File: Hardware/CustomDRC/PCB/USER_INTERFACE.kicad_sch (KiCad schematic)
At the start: 35 parts, among them J501 Conn_01x05, J504 Conn_01x05, Q501 AO3401A, Q502 AO3400A, U501 ESD224DQA, U502 ESD224DQA

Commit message: Update - finished schematic for revision A
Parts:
- removed Q501: AO3401A, Package_TO_SOT_SMD:SOT-23, symbol Transistor_FET:AO3401A
- removed Q502: AO3400A, Package_TO_SOT_SMD:SOT-23, symbol Transistor_FET:AO3400A
- added J502: JST-PH-2.0-02, Connector_JST:JST_PH_B2B-PH-K_1x02_P2.00mm_Vertical, symbol Connector_Generic:Conn_01x02
- added Q501: AO3400A, Package_TO_SOT_SMD:SOT-23, symbol Transistor_FET:AO3400A
- C501, C502, C503, C504, C505, C506: LCSC (none) -> C14663; MPN (none) -> CC0603KRX7R9BB104; Manufacturer (none) -> YAGEO
- J501, J504: value Conn_01x05 -> JST-PH-2.0-05; LCSC (none) -> C157993; MPN (none) -> B5B-PH-K-S(LF)(SN); Manufacturer (none) -> JST
- R501, R503: value 10k -> 330R; LCSC (none) -> C23138; MPN (none) -> 0603WAF3300T5E; Manufacturer (none) -> UNI-ROYAL(Uniroyal Elec)
- R502, R504, R510, R511, R512, R515: value 330R -> 10k; LCSC (none) -> C25804; MPN (none) -> 0603WAF1002T5E; Manufacturer (none) -> UNI-ROYAL(Uniroyal Elec)
- R505, R506, R507, R508, R509, R513, R514: LCSC (none) -> C25804; MPN (none) -> 0603WAF1002T5E; Manufacturer (none) -> UNI-ROYAL(Uniroyal Elec)
- TP508: footprint TestPoint:TestPoint_Pad_D1.5mm -> TestPoint:TestPoint_Keystone_5000-5004_Miniature; LCSC (none) -> C5199801; MPN (none) -> RH-5001; Manufacturer (none) -> ronghe; now in the parts list
- U501, U502: LCSC (none) -> C5199157; MPN (none) -> RClAMP3324P-ES; Manufacturer (none) -> ElecSuper
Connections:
- net VCC_ENCODER is gone; now on net VCC: R506.2, R507.2, R508.2, R509.2
- net ENCODER_1_A: no longer R506.1
- net ENCODER_1_B: now also R502.1; no longer R502.2, R507.1
- net ENCODER_1_SW: now also R512.1; no longer R512.2, R513.1
- net ENCODER_2_A: no longer R509.1
- net ENCODER_2_B: now also R510.1; no longer R508.1, R510.2
- net ENCODER_2_SW: now also R515.1; no longer R514.1, R515.2
- net ENC_1_A: now also R506.1
- net ENC_1_B: now also R502.2, R507.1; no longer R502.1
- net ENC_1_SW: now also R512.2, R513.1; no longer R512.1
- net ENC_2_B: now also R508.1, R510.2; no longer R510.1
- net ENC_2_SW: now also R514.1, R515.2; no longer R515.1
- net GND: now also R505.1, Q501.2 (S); no longer R503.2
- net VCC: no longer R501.1
- net at R501.2: now also J502.2 (Pin_2)
- net ENCODER_PWR_EN: no longer names the net of R505.2
- net ENCODER_PWR_EN: now also R503.2, Q501.1 (G); no longer R503.1
- net ENC_3_A renamed ENC_2_A
- net ENC_2_A: now also R509.1
- new net: J502.1 (Pin_1), Q501.3 (D)
- new net +5V: R501.1
- new net LED_PWM: R503.1
- no-connect marks 3 -> 2
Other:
- note added: "OUTPUT LED CONNECTOR"
- company: (none) -> JS HW
- title: (none) -> CDRC - Custom DRC for Audison AC Link
- moved on the sheet: C501, C502, C503, C504, C505, C506, J501, J504, R506, R507, R508, R509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

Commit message: Sync HW changes for V1 PCB
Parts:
- added R516: 330R, Resistor_SMD:R_1206_3216Metric_Pad1.30x1.75mm_HandSolder, symbol Device:R_Small
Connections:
- net +5V is gone; now on net VCC: R501.1
- net VCC: now also R516.2
- net at J502.2 (Pin_2), R501.2: now also R516.1
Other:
- note added: "DNP - USE IF THERMAL ISSUE"
- note added: "I = 10mA P = 0.033W"
- moved on the sheet: C501, C502, C503, C504, C505, C506, J501, J504, R501, R502, R504, R506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

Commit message: Sync before making breaking changes to RS485 comms protocl and method
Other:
- title: CDRC - Custom DRC for Audison AC Link -> CDRC - Custom DRC for Bit 10D
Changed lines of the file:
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@@
 	(paper "A4")
 	(title_block
-		(title "CDRC - Custom DRC for Audison AC Link")
-		(date "03-09-2024")
-		(rev "A")
+		(title "CDRC - Custom DRC for Bit 10D")
+		(date "01-11-2024")
+		(rev "B")
 		(company "JS HW")
 	)

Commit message: Sync changes to Rev B HW
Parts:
- removed J501, J504: JST-PH-2.0-05, Connector_JST:JST_PH_B5B-PH-K_1x05_P2.00mm_Vertical, symbol Connector_Generic:Conn_01x05
- removed J502: JST-PH-2.0-02, Connector_JST:JST_PH_B2B-PH-K_1x02_P2.00mm_Vertical, symbol Connector_Generic:Conn_01x02
- removed TP507: TestPoint_Small, TestPoint:TestPoint_Pad_D1.5mm, symbol Connector:TestPoint_Small
- added J501, J504: JST_PH_S5B-PH-SM4, Connector_JST:JST_PH_S5B-PH-SM4-TB_1x05-1MP_P2.00mm_Horizontal, symbol Connector_Generic_MountingPin:Conn_01x05_MountingPin
- added J502: ST_PH_S2B-PH-SM4, Connector_JST:JST_PH_S2B-PH-SM4-TB_1x02-1MP_P2.00mm_Horizontal, symbol Connector_Generic_MountingPin:Conn_01x02_MountingPin
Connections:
- net ENC_1_A: now also J501.1 (Pin_1)
- net ENC_1_B: now also J501.3 (Pin_3)
- net ENC_1_SW: now also J501.5 (Pin_5)
- net ENC_2_A: now also J504.1 (Pin_1)
- net ENC_2_B: now also J504.3 (Pin_3)
- net ENC_2_SW: now also J504.5 (Pin_5)
- net GND: now also J501.2 (Pin_2), J501.4 (Pin_4), J504.2 (Pin_2), J504.4 (Pin_4)
- net at Q501.3 (D): now also J502.1 (Pin_1)
- net at R501.2, R516.1: now also J502.2 (Pin_2)
- new net MNT: J501.MP (MountPin), J502.MP (MountPin), J504.MP (MountPin)
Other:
- note added: "ENCODERS"
- note added: "LED CONTROL"
- moved on the sheet: Q501, R501, R503, R505, R516

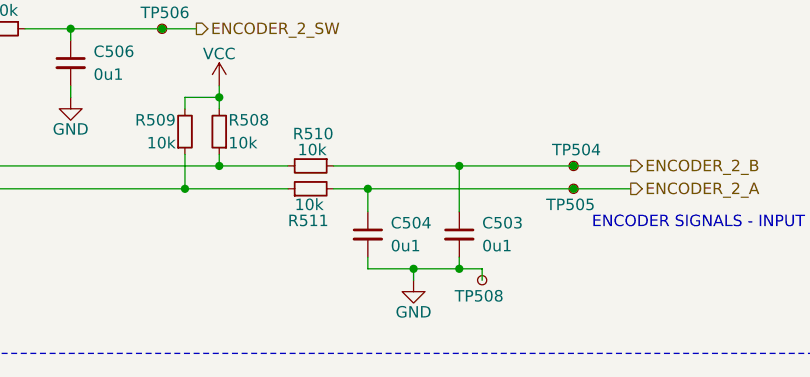
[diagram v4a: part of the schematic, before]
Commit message: Added board renders and PDF plots
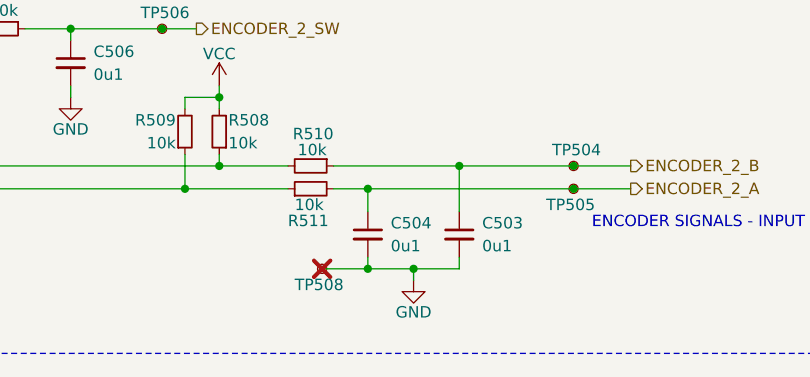
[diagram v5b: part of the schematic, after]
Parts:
- TP508: now not fitted; now left out of the parts list
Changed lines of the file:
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@@
 	)
 	(junction
+		(at 167.64 147.32)
+		(diameter 0)
+		(color 0 0 0 0)
+	)
+	(junction
 		(at 121.92 77.47)
 		(diameter 0)
@@
 	)
 	(junction
-		(at 177.8 147.32)
-		(diameter 0)
-		(color 0 0 0 0)
-	)
-	(junction
 		(at 120.65 120.65)
 		(diameter 0)
@@
 	(wire
 		(pts
-			(xy 172.72 147.32) (xy 167.64 147.32)
-		)
-		(stroke
-			(width 0)
-			(type default)
-		)
-	)
-	(wire
-		(pts
 			(xy 87.63 41.91) (xy 87.63 43.18)
 		)
@@
 	(wire
 		(pts
-			(xy 177.8 147.32) (xy 180.34 147.32)
+			(xy 162.56 147.32) (xy 167.64 147.32)
 		)
 		(stroke
@@
 	(wire
 		(pts
-			(xy 180.34 148.59) (xy 180.34 147.32)
+			(xy 167.64 147.32) (xy 172.72 147.32)
 		)
 		(stroke
@@
 	(symbol
 		(lib_id "Connector:TestPoint_Small")
-		(at 180.34 148.59 0)
+		(at 162.56 147.32 0)
 		(mirror x)
 		(unit 1)
 		(exclude_from_sim no)
-		(in_bom yes)
+		(in_bom no)
 		(on_board yes)
-		(dnp no)
+		(dnp yes)
 		(property "Reference" "TP508"
-			(at 177.292 150.368 0)
+			(at 159.512 149.098 0)
 			(effects
 				(font
@@
 		)
 		(property "Value" "TestPoint_Small"
-			(at 181.61 147.3201 0)
+			(at 163.83 146.0501 0)
 			(effects
 				(font
@@
 		)
 		(property "Footprint" "TestPoint:TestPoint_Keystone_5000-5004_Miniature"
-			(at 185.42 148.59 0)
+			(at 167.64 147.32 0)
 			(effects
 				(font
@@
 		)
 		(property "Datasheet" "~"
-			(at 185.42 148.59 0)
+			(at 167.64 147.32 0)
 			(effects
 				(font
@@
 		)
 		(property "Description" "test point"
-			(at 180.34 148.59 0)
+			(at 162.56 147.32 0)
 			(effects
 				(font
@@
 		)
 		(property "LCSC" "C5199801"
-			(at 180.34 148.59 0)
+			(at 162.56 147.32 0)
 			(effects
 				(font
@@
 		)
 		(property "MPN" " RH-5001"
-			(at 180.34 148.59 0)
+			(at 162.56 147.32 0)
 			(effects
 				(font
@@
 		)
 		(property "Manufacturer" " ronghe"
-			(at 180.34 148.59 0)
+			(at 162.56 147.32 0)
 			(effects
 				(font

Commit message: Update HW folder with latest work on rev B
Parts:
- J501, J504: LCSC (none) -> C265104; MPN (none) -> S5B-PH-SM4-TB(LF)(SN); Manufacturer (none) -> JST
- J502: value ST_PH_S2B-PH-SM4 -> JST_PH_S2B-PH-SM4; LCSC (none) -> C295747; MPN (none) -> S2B-PH-SM4-TB(LF)(SN); Manufacturer (none) -> JST
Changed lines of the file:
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@@
 	(title_block
 		(title "CDRC - Custom DRC for Bit 10D")
-		(date "01-11-2024")
+		(date "25-11-2024")
 		(rev "B")
 		(company "JS HW")
@@
 			)
 		)
-		(property "Value" "ST_PH_S2B-PH-SM4"
+		(property "Value" "JST_PH_S2B-PH-SM4"
 			(at 97.79 39.116 0)
 			(effects
@@
 			)
 		)
+		(property "Manufacturer" "JST"
+			(at 95.25 41.91 0)
+			(effects
+				(font
+					(size 1.27 1.27)
+				)
+				(hide yes)
+			)
+		)
+		(property "MPN" " S2B-PH-SM4-TB(LF)(SN)"
+			(at 95.25 41.91 0)
+			(effects
+				(font
+					(size 1.27 1.27)
+				)
+				(hide yes)
+			)
+		)
+		(property "LCSC" "C295747"
+			(at 95.25 41.91 0)
+			(effects
+				(font
+					(size 1.27 1.27)
+				)
+				(hide yes)
+			)
+		)
 		(pin "1"
 		)
@@
 			)
 		)
+		(property "LCSC" "C265104"
+			(at 73.66 130.81 0)
+			(effects
+				(font
+					(size 1.27 1.27)
+				)
+				(hide yes)
+			)
+		)
+		(property "MPN" "S5B-PH-SM4-TB(LF)(SN)"
+			(at 73.66 130.81 0)
+			(effects
+				(font
+					(size 1.27 1.27)
+				)
+				(hide yes)
+			)
+		)
+		(property "Manufacturer" "JST"
+			(at 73.66 130.81 0)
+			(effects
+				(font
+					(size 1.27 1.27)
+				)
+				(hide yes)
+			)
+		)
 		(pin "3"
 		)
@@
 			(at 73.66 87.63 0)
 			(effects
+				(font
+					(size 1.27 1.27)
+				)
+				(hide yes)
+			)
+		)
+		(property "LCSC" "C265104"
+			(at 73.66 87.63 0)
+			(effects
+				(font
+					(size 1.27 1.27)
+				)
+				(hide yes)
+			)
+		)
+		(property "MPN" "S5B-PH-SM4-TB(LF)(SN)"
+			(at 73.66 87.63 0)
+			(effects
+				(font
+					(size 1.27 1.27)
+				)
+				(hide yes)
+			)
+		)
+		(property "Manufacturer" "JST"
+			(at 73.66 87.63 0)
+			(effects
